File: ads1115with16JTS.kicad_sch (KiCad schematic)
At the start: 50 parts, among them J1 Conn_01x02_Pin, J10 Conn_01x02_Pin, J11 Conn_01x02_Pin, J12 Conn_01x02_Pin, J13 Conn_01x02_Pin, J14 Conn_01x02_Pin, J15 Conn_01x02_Pin, J16 Conn_01x02_Pin, J17 Conn_01x04_Pin, J18 PinSocket_1x20_P2.54mm_Vertic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, J19 PinSocket_1x20_P2.54mm_Vertic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, J2 Conn_01x02_Pin, J20 Screw_Terminal_01x02, J3 Conn_01x02_Pin, J4 Conn_01x02_Pin, J5 Conn_01x02_Pin, J6 Conn_01x02_Pin, J7 Conn_01x02_Pin, J8 Conn_01x02_Pin, J9 Conn_01x02_Pin, U1 ADS1115IDGS, U2 ADS1115IDGS, U3 ADS1115IDGS, U4 ADS1115IDGS

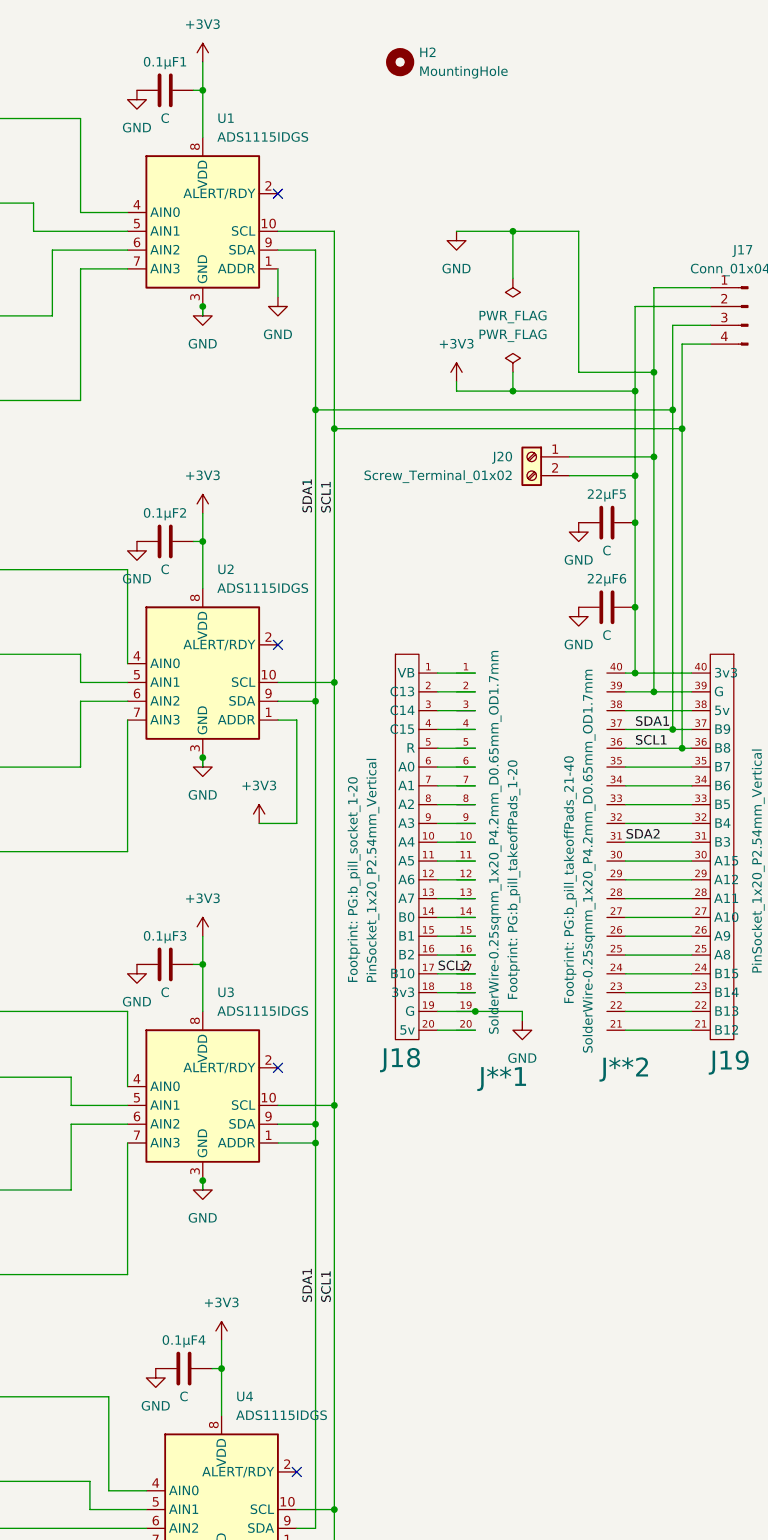
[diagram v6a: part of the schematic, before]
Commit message: footprint lib adjustments.
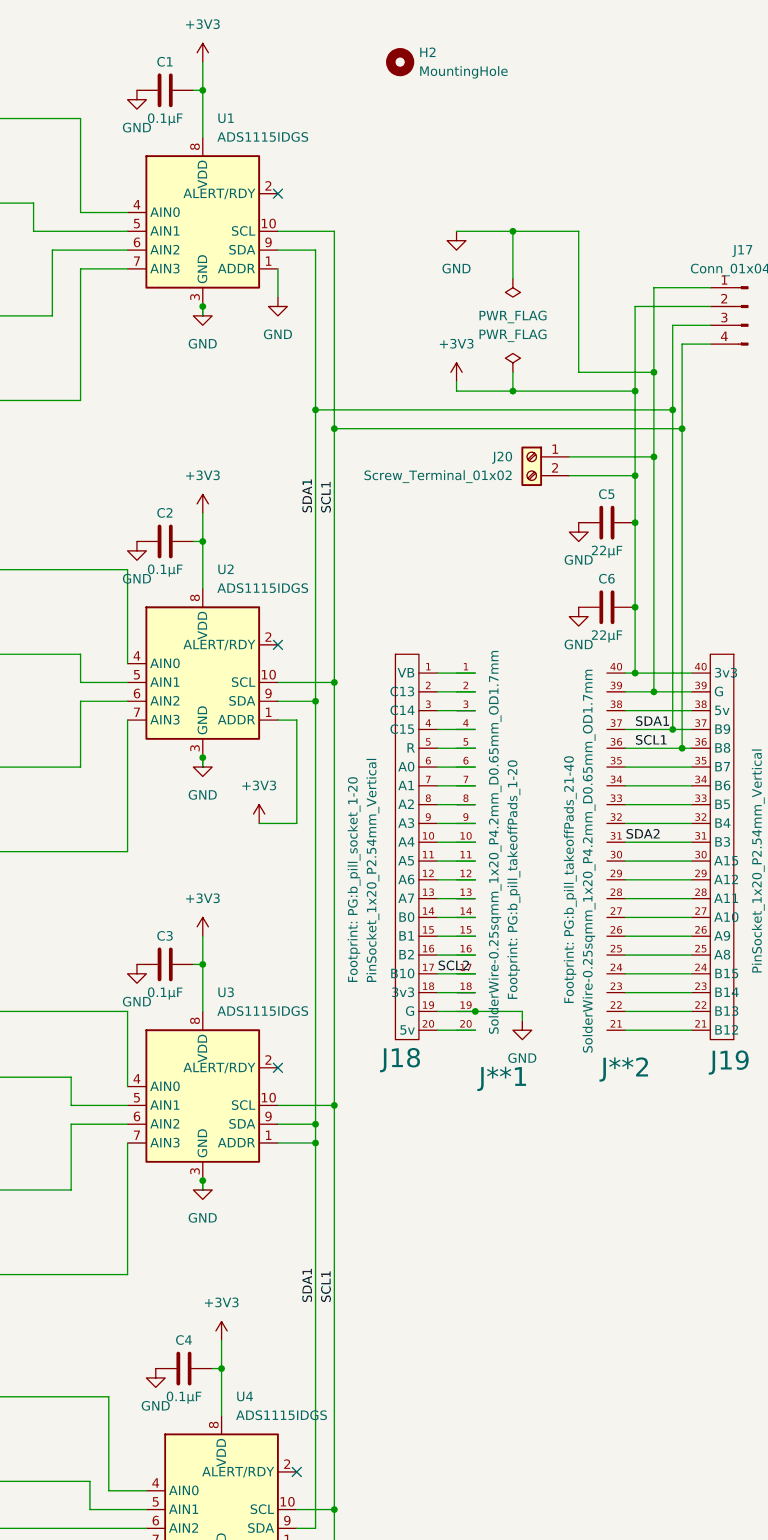
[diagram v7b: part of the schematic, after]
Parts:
- C1: renamed from 0.1µF1; value C -> 0.1µF
- C2: renamed from 0.1µF2; value C -> 0.1µF
- C3: renamed from 0.1µF3; value C -> 0.1µF
- C4: renamed from 0.1µF4; value C -> 0.1µF
- C5: renamed from 22µF5; value C -> 22µF
- C6: renamed from 22µF6; value C -> 22µF
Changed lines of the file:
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@@
   (symbol (lib_id "ProjectLib:C") (at 120.65 85.09 270) (mirror x) (unit 1)
     (in_bom yes) (on_board yes) (dnp no)
-    (property "Reference" "0.1µF2" (at 120.65 81.28 90)
-      (effects (font (size 1.27 1.27)))
-    )
-    (property "Value" "C" (at 120.65 88.9 90)
+    (property "Reference" "C2" (at 120.65 81.28 90)
+      (effects (font (size 1.27 1.27)))
+    )
+    (property "Value" "0.1µF" (at 120.65 88.9 90)
       (effects (font (size 1.27 1.27)))
     )
@@
       (project "ads1115with16JTS"
         (path "/0c2d0c14-8850-4a30-bb78-b2f40cb442ba"
-          (reference "0.1µF2") (unit 1)
+          (reference "C2") (unit 1)
         )
       )
@@
   (symbol (lib_id "ProjectLib:C") (at 180.34 93.98 270) (mirror x) (unit 1)
     (in_bom yes) (on_board yes) (dnp no)
-    (property "Reference" "22µF6" (at 180.34 90.17 90)
-      (effects (font (size 1.27 1.27)))
-    )
-    (property "Value" "C" (at 180.34 97.79 90)
+    (property "Reference" "C6" (at 180.34 90.17 90)
+      (effects (font (size 1.27 1.27)))
+    )
+    (property "Value" "22µF" (at 180.34 97.79 90)
       (effects (font (size 1.27 1.27)))
     )
@@
       (project "ads1115with16JTS"
         (path "/0c2d0c14-8850-4a30-bb78-b2f40cb442ba"
-          (reference "22µF6") (unit 1)
+          (reference "C6") (unit 1)
         )
       )
@@
   (symbol (lib_id "ProjectLib:C") (at 120.65 24.13 270) (mirror x) (unit 1)
     (in_bom yes) (on_board yes) (dnp no)
-    (property "Reference" "0.1µF1" (at 120.65 20.32 90)
-      (effects (font (size 1.27 1.27)))
-    )
-    (property "Value" "C" (at 120.65 27.94 90)
+    (property "Reference" "C1" (at 120.65 20.32 90)
+      (effects (font (size 1.27 1.27)))
+    )
+    (property "Value" "0.1µF" (at 120.65 27.94 90)
       (effects (font (size 1.27 1.27)))
     )
@@
       (project "ads1115with16JTS"
         (path "/0c2d0c14-8850-4a30-bb78-b2f40cb442ba"
-          (reference "0.1µF1") (unit 1)
+          (reference "C1") (unit 1)
         )
       )
@@
   (symbol (lib_id "ProjectLib:C") (at 123.19 196.85 270) (mirror x) (unit 1)
     (in_bom yes) (on_board yes) (dnp no)
-    (property "Reference" "0.1µF4" (at 123.19 193.04 90)
-      (effects (font (size 1.27 1.27)))
-    )
-    (property "Value" "C" (at 123.19 200.66 90)
+    (property "Reference" "C4" (at 123.19 193.04 90)
+      (effects (font (size 1.27 1.27)))
+    )
+    (property "Value" "0.1µF" (at 123.19 200.66 90)
       (effects (font (size 1.27 1.27)))
     )
@@
       (project "ads1115with16JTS"
         (path "/0c2d0c14-8850-4a30-bb78-b2f40cb442ba"
-          (reference "0.1µF4") (unit 1)
+          (reference "C4") (unit 1)
         )
       )
@@
   (symbol (lib_id "ProjectLib:C") (at 120.65 142.24 270) (mirror x) (unit 1)
     (in_bom yes) (on_board yes) (dnp no)
-    (property "Reference" "0.1µF3" (at 120.65 138.43 90)
-      (effects (font (size 1.27 1.27)))
-    )
-    (property "Value" "C" (at 120.65 146.05 90)
+    (property "Reference" "C3" (at 120.65 138.43 90)
+      (effects (font (size 1.27 1.27)))
+    )
+    (property "Value" "0.1µF" (at 120.65 146.05 90)
       (effects (font (size 1.27 1.27)))
     )
@@
       (project "ads1115with16JTS"
         (path "/0c2d0c14-8850-4a30-bb78-b2f40cb442ba"
-          (reference "0.1µF3") (unit 1)
+          (reference "C3") (unit 1)
         )
       )
@@
   (symbol (lib_id "ProjectLib:C") (at 180.34 82.55 270) (mirror x) (unit 1)
     (in_bom yes) (on_board yes) (dnp no)
-    (property "Reference" "22µF5" (at 180.34 78.74 90)
-      (effects (font (size 1.27 1.27)))
-    )
-    (property "Value" "C" (at 180.34 86.36 90)
+    (property "Reference" "C5" (at 180.34 78.74 90)
+      (effects (font (size 1.27 1.27)))
+    )
+    (property "Value" "22µF" (at 180.34 86.36 90)
       (effects (font (size 1.27 1.27)))
     )
@@
       (project "ads1115with16JTS"
         (path "/0c2d0c14-8850-4a30-bb78-b2f40cb442ba"
-          (reference "22µF5") (unit 1)
-        )
-      )
+          (reference "C5") (unit 1)
+        )
+      )
